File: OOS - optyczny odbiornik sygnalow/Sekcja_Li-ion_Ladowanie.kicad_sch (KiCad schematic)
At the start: 0 parts

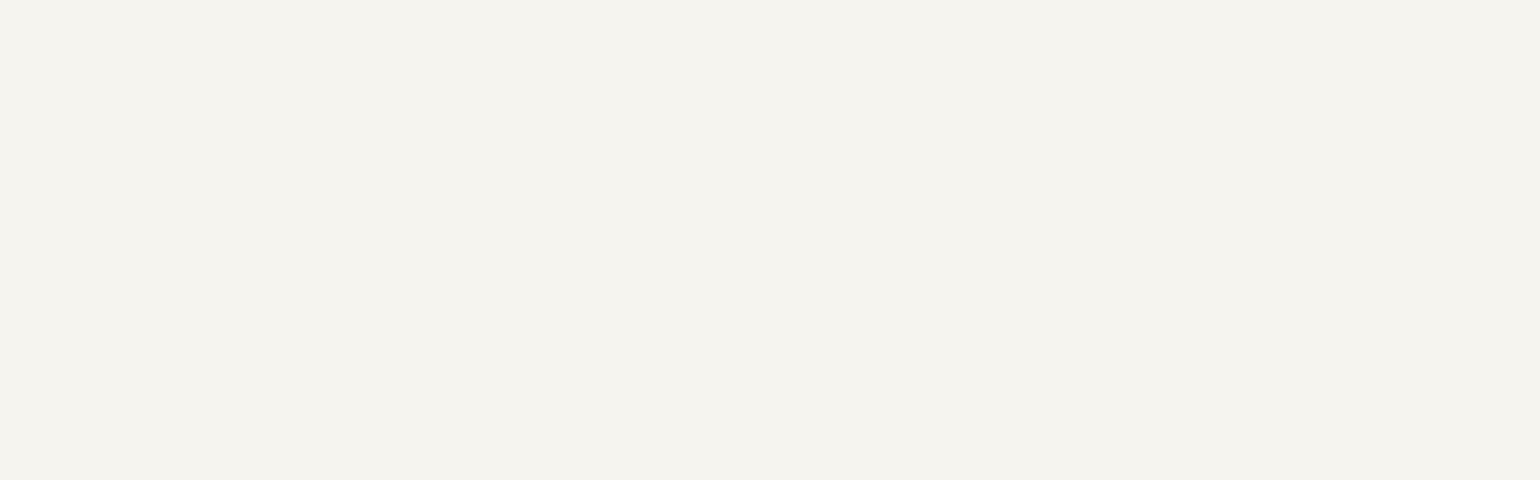
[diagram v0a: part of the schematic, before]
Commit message: Add Charging, protection circuit and LDO for +3V3 with passive, transistor and diode components
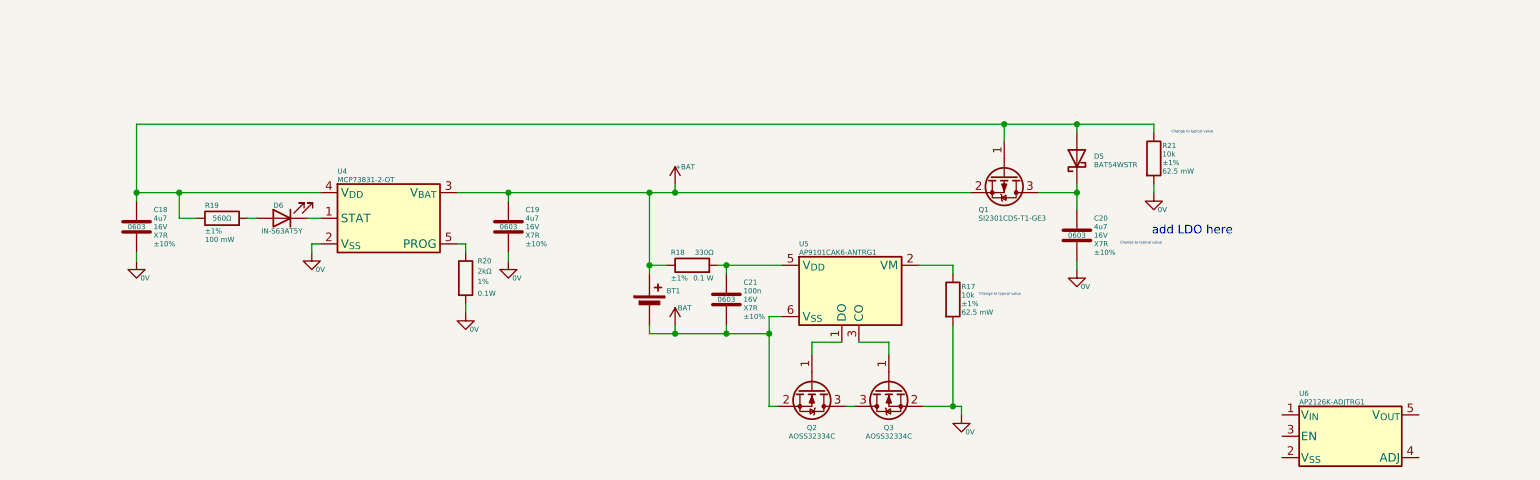
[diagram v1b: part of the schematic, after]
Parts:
- added BT1: Battery_Cell, Battery:BatteryHolder_MPD_BH-18650-PC2, symbol Device:Battery_Cell
- added C18, C19, C20: 4u7, Capacitor_SMD:C_0603_1608Metric, symbol Device:C
- added C21: 100n, Capacitor_SMD:C_0603_1608Metric_Pad1.08x0.95mm_HandSolder, symbol Device:C
- added D5: BAT54WSTR, Diode_SMD:D_SOD-323, symbol Diode:BAT54J
- added D6: LED, Diode_SMD:D_0603_1608Metric_Pad1.05x0.95mm_HandSolder, symbol Device:LED
- added Q1: SI2301CDS-T1-GE3, Package_TO_SOT_SMD:SOT-23_Handsoldering, symbol Transistor_FET:Si2319CDS
- added Q2, Q3: AOSS32334C, Package_TO_SOT_SMD:SOT-23, symbol Transistor_FET:AO3400A
- added R17, R21: 10k, Resistor_SMD:R_0402_1005Metric_Pad0.72x0.64mm_HandSolder, symbol Device:R
- added R18: 330Ω, Resistor_SMD:R_0603_1608Metric_Pad0.98x0.95mm_HandSolder, symbol Device:R
- added R19: 560Ω, Resistor_SMD:R_0603_1608Metric_Pad0.98x0.95mm_HandSolder, symbol Device:R
- added R20: 2kΩ, Resistor_SMD:R_0603_1608Metric_Pad0.98x0.95mm_HandSolder, symbol Device:R
- added U4: MCP73831-2-OT, Package_TO_SOT_SMD:SOT-23-5, symbol Battery_Management:MCP73831-2-OT
- added U5: AP9101CAK6-ANTRG1, Package_TO_SOT_SMD:SOT-23-6, symbol Battery_Management:AP9101CK6
- added U6: AP2126K-ADJTRG1, Package_TO_SOT_SMD:SOT-23-5_HandSoldering, symbol Regulator_Linear:AP2127K-3.3
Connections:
- new net: C18.1, D5.2 (A), Q1.1 (G), R19.1, R21.1, U4.4 (V_{DD})
- new net: D6.2 (A), R19.2
- new net: C20.1, D5.1 (K), Q1.3 (D)
- new net: R17.1, U5.2 (VM)
- new net: D6.1 (K), U4.1 (STAT)
- new net: R20.1, U4.5 (PROG)
- new net: Q2.1 (G), U5.1 (DO)
- new net: Q3.1 (G), U5.3 (CO)
- new net: C21.1, R18.2, U5.5 (V_{DD})
- new net: Q2.3 (D), Q3.3 (D)
- new net +BAT: BT1.1 (+), C19.1, Q1.2 (S), R18.1, U4.3 (V_{BAT})
- new net -BAT: BT1.2 (-), C21.2, Q2.2 (S), U5.6 (V_{SS})
- new net 0V: C18.2, C19.2, C20.2, Q3.2 (S), R17.2, R20.2, R21.2, U4.2 (V_{SS})
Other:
- note added: "Change to typical value"
- note added: "add LDO here"

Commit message: Finish Li-Lion section, add for review
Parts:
- added C17, C22: 1u, Capacitor_SMD:C_0603_1608Metric_Pad1.08x0.95mm_HandSolder, symbol Device:C
- added J1: Conn_01x02_Pin, Connector_PinHeader_2.54mm:PinHeader_1x02_P2.54mm_Vertical, symbol Connector:Conn_01x02_Pin
- added R12, R25: 0R, Resistor_SMD:R_0603_1608Metric, symbol Device:R
- added R22: 10k, Resistor_SMD:R_0402_1005Metric_Pad0.72x0.64mm_HandSolder, symbol Device:R
- added R23: 40k2, Resistor_SMD:R_0603_1608Metric, symbol Device:R
- added R24: 24k3, Resistor_SMD:R_0603_1608Metric, symbol Device:R
- added TP18, TP19, TP20, TP21, TP22, TP23, TP24, TP25, TP26, TP27, TP28, TP29, TP30, TP31, TP32: TestPoint_Small, TestPoint:TestPoint_Pad_D1.0mm, symbol Connector:TestPoint_Small
- C20: now not fitted
- Q2, Q3: Rds max (none) -> 26m; Rds typ (none) -> 20m
- R17: value 10k -> 2k7; footprint Resistor_SMD:R_0402_1005Metric_Pad0.72x0.64mm_HandSolder -> Resistor_SMD:R_0603_1608Metric_Pad0.98x0.95mm_HandSolder; MPN WR04X1002FTL -> ERJ3EKF2701V; Package 0402 -> 0603; Power Rating 62.5 mW -> 0.1 W; Supplier Link https://www.tme.eu/pl/details/wr04x1002ftl/rezystory-smd/wa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 -> https://www.tme.eu/pl/details/erj3ekf2701v/rezystory-smd/pa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
- R18: value 330Ω -> 330
- R19: value 560Ω -> 560
- R20: value 2kΩ -> 2k
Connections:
- net +BAT: now also TP21.1
- net -BAT: now also TP23.1
- net 0V: now also U6.2 (V_{SS}), C17.2, C22.2, J1.2 (Pin_2), R24.2
- net +5V: now reaches D5.2 (A), Q1.1 (G), R21.1
- net +5V: now also R25.2; no longer C18.1, R19.1, U4.4 (V_{DD})
- net D5_A: now reaches D6.2 (A), R19.2
- net D5_A: now also TP19.1
- net U6_V_{IN}: now reaches U6.1 (V_{IN})
- net U6_V_{IN}: now also C20.1, D5.1 (K), Q1.3 (D), C17.1, R22.1, TP29.1
- net U6_EN: now reaches U6.3 (EN)
- net U6_EN: now also J1.1 (Pin_1), R22.2, TP30.1
- net U6_ADJ: now reaches U6.4 (ADJ)
- net U6_ADJ: now also R23.2, R24.1, TP31.1
- net at U6.5 (V_{OUT}): now also C22.1, R12.1, R23.1, TP32.1
- net U5_VM: now reaches R17.1, U5.2 (VM)
- net U5_VM: now also TP25.1
- net U3_STAT: now reaches D6.1 (K), U4.1 (STAT)
- net U3_STAT: now also TP20.1
- net U3_PROG: now reaches R20.1, U4.5 (PROG)
- net U3_PROG: now also TP22.1
- net U5_DO: now reaches Q2.1 (G), U5.1 (DO)
- net U5_DO: now also TP27.1
- net U5_CO: now reaches Q3.1 (G), U5.3 (CO)
- net U5_CO: now also TP28.1
- net U5_V_{DD}: now reaches C21.1, R18.2, U5.5 (V_{DD})
- net U5_V_{DD}: now also TP24.1
- net Q2/Q3_D: now reaches Q2.3 (D), Q3.3 (D)
- net Q2/Q3_D: now also TP26.1
- new net +3V3: R12.2
- new net U3_V_{DD}: C18.1, R19.1, R25.1, TP18.1, U4.4 (V_{DD})
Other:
- note added: "170mV@300mA for VOUT = 3.3V"
- note added: "CC - 500mA CV - 4.2V"
- note added: "Vin 1V5 to 5V5"
- note added: "Vin 3V to 6V"
- note added: "Vin 3V75 to 6V"
- note removed: "Change to typical value"
- note removed: "add LDO here"
- moved on the sheet: BT1, C18, C19, C21, D5, D6, Q1, Q2, Q3, R17, R18, R19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

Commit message: Internal changes
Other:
- note added: "Take voltage for boost converter from here"
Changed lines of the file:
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@@
+		)
+	)
+	(text "Take voltage for boost converter from here"
+		(exclude_from_sim no)
+		(at 193.675 77.47 90)
+		(effects
+			(font
+				(size 0.635 0.635)
+				(thickness 0.127)
+				(bold yes)
+				(color 255 0 0 1)
+			)
 		)
 	)
